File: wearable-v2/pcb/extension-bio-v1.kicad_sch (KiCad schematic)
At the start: 10 parts, among them J6 HERALD_V2_CONN_PLUG, U11 TMP1075, U12 MAX30102

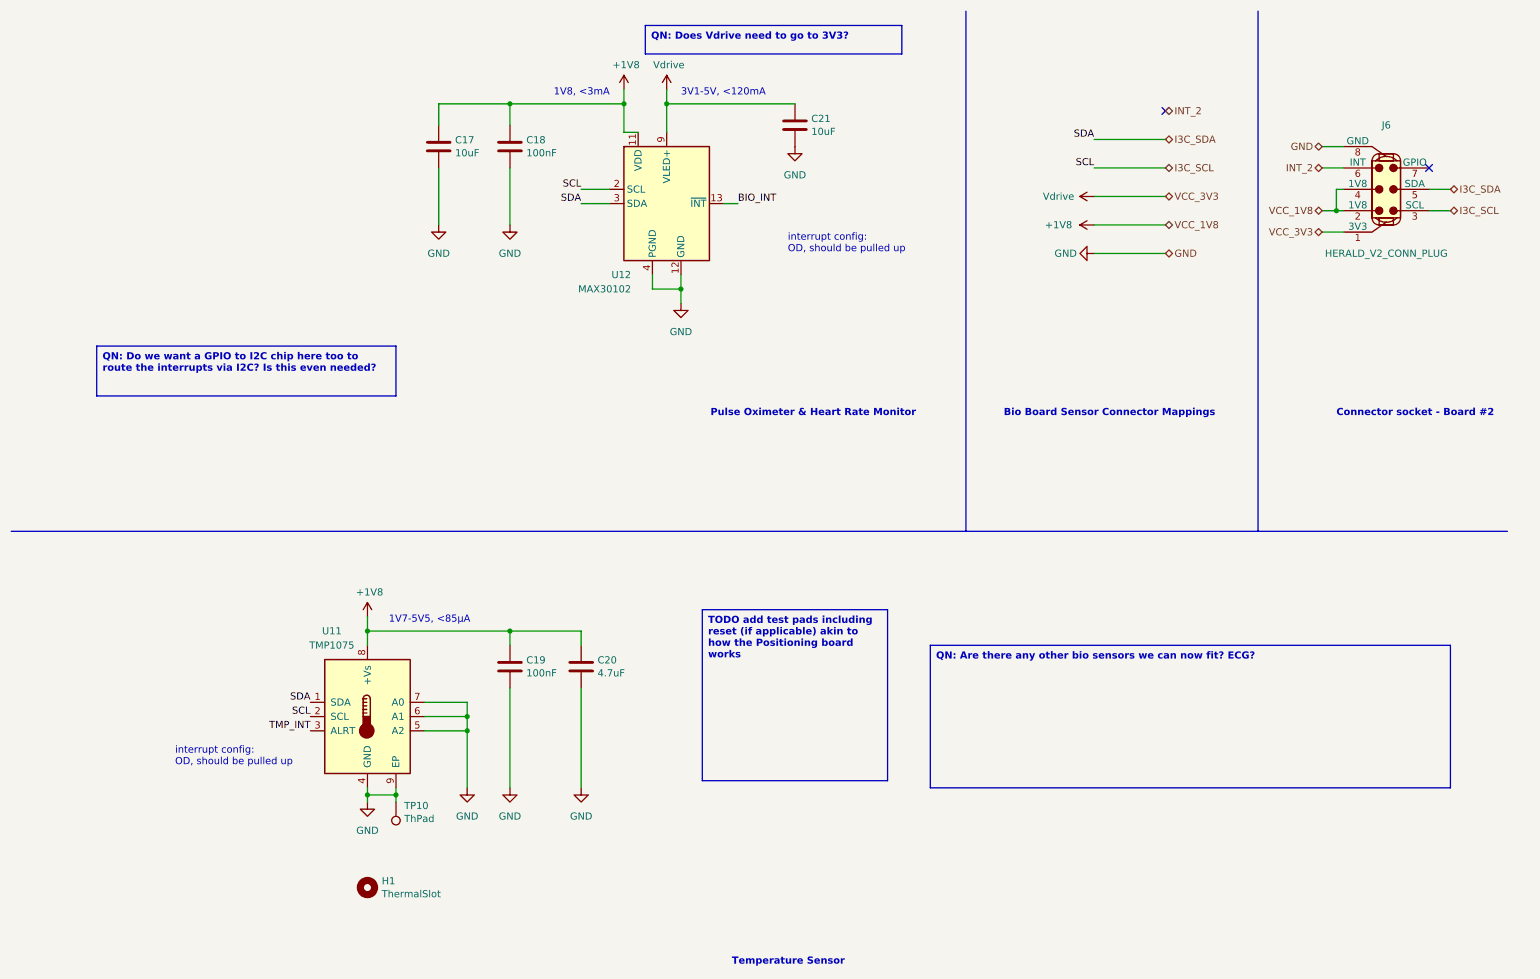
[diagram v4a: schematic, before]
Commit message: Added I2C and I3C notes and additional resistors
Signed-off-by: Adam Fowler <adam@adamfowler.org>
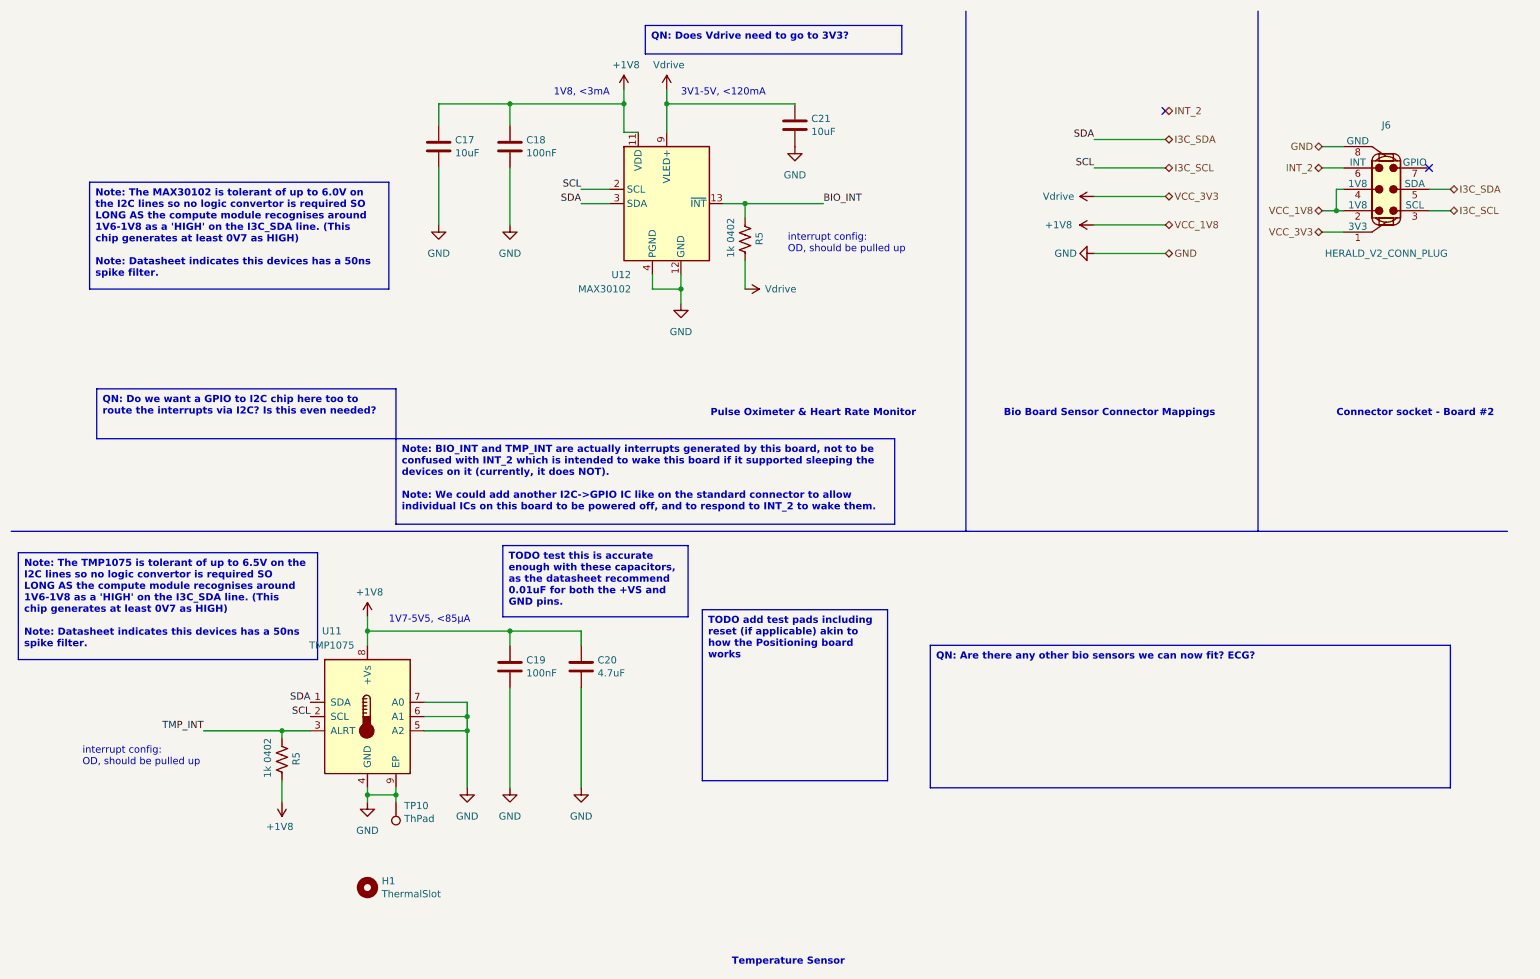
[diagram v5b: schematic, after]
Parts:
- added R5 (x2): 1k 0402, Resistor_SMD:R_0402_1005Metric, symbol Device:R_US
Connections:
- net +1V8: now also R5.1
- net BIO_INT: now also R5.2
- net TMP_INT: now also R5.2
- net Vdrive: now also R5.1
